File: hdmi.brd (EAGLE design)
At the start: 160 x 100 mm, 143 parts, among them IC1 FT2232HQ, Q1 N-MOSFETSOT23, U0 6SLX45CSG324, U1 MT41J64M16, U2 TPD12S016RKTR, U3 TPD12S016RKTR, U4 TPD12S016RKTR, U5 MNR18, U6 MNR18, U8 20Mhz

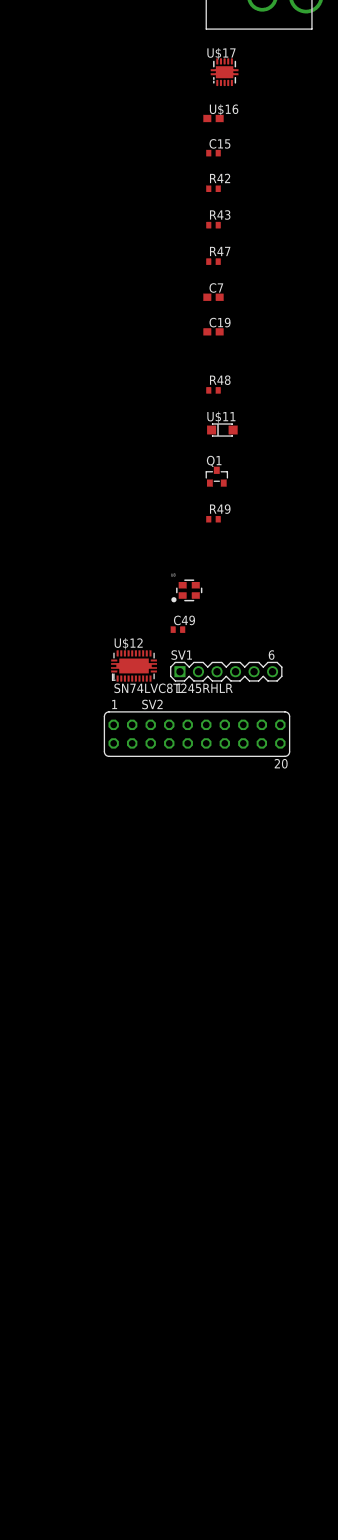
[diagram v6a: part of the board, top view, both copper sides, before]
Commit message: switched from hot swap controller to buck regulator, +PMOD
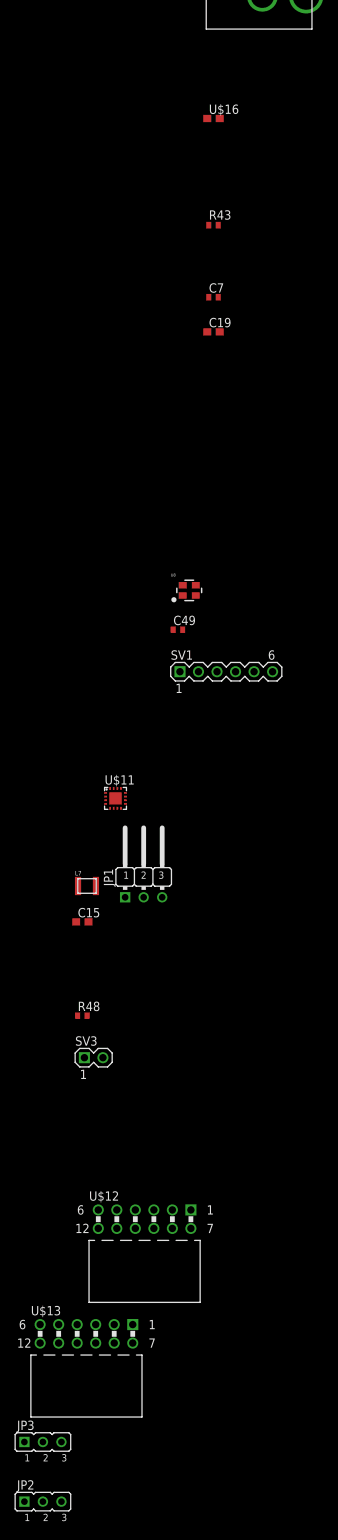
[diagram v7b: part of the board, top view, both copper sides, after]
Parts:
- removed Q1: N-MOSFETSOT23, prj-hdmi:SOT23
- removed R42: 47k, resistor:R0402
- removed R47, R49: 1k, resistor:R0402
- removed SV2: FE10-2, prj-hdmi:FE10-2
- removed U$17: TPS2592BA, prj-hdmi:DRC-S-PVSON-N10
- added JP1: 5V_SEL, prj-hdmi:JP2W
- added JP2: PMOD0-1_VCC_SEL, prj-hdmi:JP2
- added JP3: PMOD2-3_VCC_SEL, prj-hdmi:JP2
- added L7: 3.3u, 4A, prj-hdmi:1008
- added SV3: EXT_SUP, prj-hdmi:MA02-1
- added U$13: PMOD-2X6, prj-hdmi:PMOD-2X6
- C15: value 0.47n -> 0.1u; device rcl:C0402 -> prj-hdmi:0603
- C19: value 0.1u -> 10u
- C7: value 100u -> 10u; device prj-hdmi:0603 -> prj-hdmi:0402
- R44: value 4.7k -> 10k
- R48: value 4.7k -> 10k; device resistor:R0402 -> prj-hdmi:0402
- U$11: value 20V -> MIC24085; device prj-hdmi:SOD123FL -> prj-hdmi:QFN-16-3X3
- U$12: value SN74LVC8T245RHLR -> PMOD-2X6; device prj-hdmi:RHL_R-PVQFN-N24 -> prj-hdmi:PMOD-2X6
- moved C15 107.0 mm to (-166.6, -834.5)
- moved R48 87.6 mm to (-166.6, -847.3)
- moved U$12 75.9 mm to (-158.0, -875.3)
- moved U$11 52.6 mm to (-162.0, -817.5)
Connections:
- removed net IO_0: SV2.5, U0.B11
- removed net IO_1: SV2.7, U0.A11
- removed net IO_10: U$12.5, U0.C15
- removed net IO_10_5V: SV2.10, U$12.19
- removed net IO_11: U$12.6, U0.A15
- removed net IO_11_5V: SV2.12, U$12.18
- removed net IO_12: U$12.7, U0.D14
- removed net IO_12_5V: SV2.14, U$12.17
- removed net IO_13: U$12.8, U0.C14
- removed net IO_13_5V: SV2.16, U$12.16
- removed net IO_14: U$12.9, U0.B16
- removed net IO_14_5V: SV2.18, U$12.15
- removed net IO_15: U$12.10, U0.A16
- removed net IO_15_5V: SV2.20, U$12.14
- removed net IO_2: SV2.9, U0.B12
- removed net IO_3: SV2.11, U0.A12
- removed net IO_4: SV2.13, U0.C13
- removed net IO_5: SV2.15, U0.A13
- removed net IO_6: SV2.17, U0.B14
- removed net IO_7: SV2.19, U0.A14
- removed net IO_8: U$12.3, U0.F13
- removed net IO_8-15_DIR: U$12.2, U0.F9
- removed net IO_8-15_DISABLE: U$12.22, U0.G9
- removed net IO_8_5V: SV2.6, U$12.21
- removed net IO_9: U$12.4, U0.E13
- removed net IO_9_5V: SV2.8, U$12.20
- removed net N$32: C15.1, U$17.1
- removed net N$36: R42.2, U$17.10
- removed net OUT@8: Q1.2, R49.2, U$17.6, U$17.7, U$17.8
- new net N$2: C15.1, U$11.10
- new net N$51: JP2.2, U$12.12, U$12.6
- new net PMOD0_0: U$12.1, U0.B11
- new net PMOD0_1: U$12.2, U0.A11
- new net PMOD0_2: U$12.3, U0.B12
- new net PMOD0_3: U$12.4, U0.A12
- new net PMOD1_0: U$12.7, U0.C13
- new net PMOD1_1: U$12.8, U0.A13
- new net PMOD1_2: U$12.9, U0.B14
- new net PMOD1_3: U$12.10, U0.A14
- new net PMOD2_0: U$13.1, U0.F13
- new net PMOD2_1: U$13.2, U0.E13
- new net PMOD2_2: U$13.3, U0.C15
- new net PMOD2_3: U$13.4, U0.A15
- new net PMOD3_0: U$13.7, U0.D14
- new net PMOD3_1: U$13.8, U0.C14
- new net PMOD3_2: U$13.9, U0.B16
- new net PMOD3_3: U$13.10, U0.A16
- new net SW@16: C15.2, L7.1, U$11.1, U$11.12, U$11.13, U$11.16
- new net USB_VBUS: JP1.3, U$10.1, U$10.2
- net +3V3: now also JP2.1, JP3.1; no longer SV2.1, U$12.1
- net +5V: now also JP1.2, JP2.3, JP3.3; no longer Q1.3, SV2.2, U$10.1, U$10.2, U$12.23, U$12.24
- net CENTER: now also SV3.1; no longer U$11.C
- net GND: now also SV3.2, U$11.14, U$11.15, U$11.4, U$11.ETP, U$12.5, U$13.11, U$13.5; no longer C15.2, R42.1, R48.1, SV2.3, SV2.4, U$11.A, U$12.12, U$12.13, U$12.ETP, U$12.ETP@1, U$12.ETP@2, U$12.ETP@3, U$17.TH, U$17.TH@1, U$17.TH@2
- net N$29: now also R48.2, U$11.11, U$11.2, U$11.3; no longer R47.2, U$17.3, U$17.4, U$17.5
- net N$30: now also JP1.1, L7.2, U$11.5; no longer R47.1, R48.2, U$17.2
- net N$49: now also JP3.2, U$13.12, U$13.6; no longer Q1.1, U$17.9
- net USB_5V_DISABLE: now also R48.1, U$11.8; no longer R49.1
